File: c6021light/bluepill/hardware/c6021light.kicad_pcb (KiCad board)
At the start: 2 copper layers, 100 x 50 mm, 82 parts, among them J1 Barrel_Jack_Switch, J10 Conn_01x02, J11 Conn_01x02, J12 XpressNet, J2 Conn_02x04_Odd_Even, J3 Conn_02x16_Row_Letter_First, J30 Loconet, J31 Conn_01x02, J32 Conn_01x02, J4 Conn_01x02, J5 Grove I2C, J50 USB_B_Micro, J51 Conn_01x06, J52 Debug UART, J6 Conn_01x02, J7 Conn_01x02, J8 RJ45, Q30 BC337, Q31 BC547, Q32 BC547, SW1 SW_Push, U1 L7805, U10 SN75176, U2 L7808, U3 MCP2562, U30 LM393, U4 ISO1050DUB, U50 CH340C

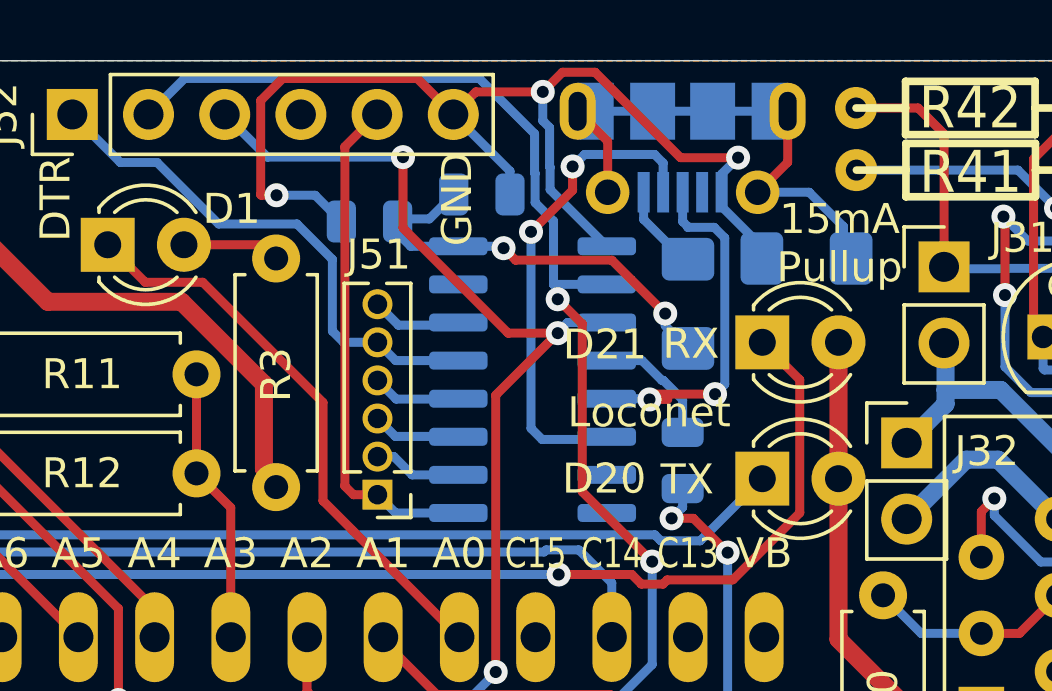
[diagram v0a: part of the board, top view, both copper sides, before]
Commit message: remove some unneccessary resistors
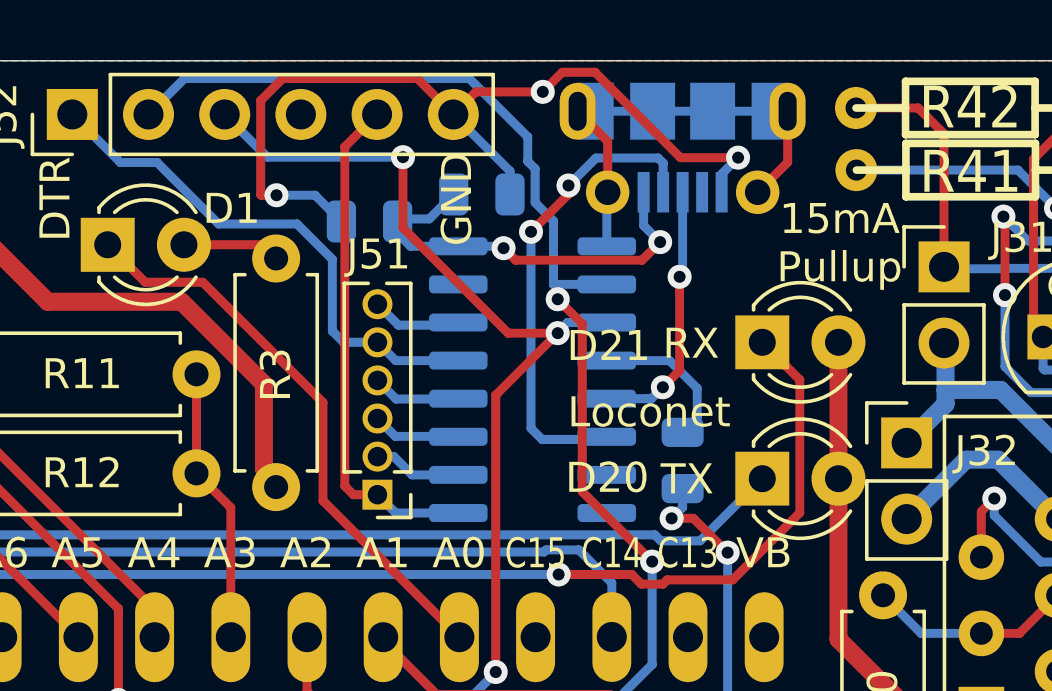
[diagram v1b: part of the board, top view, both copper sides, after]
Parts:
- removed R50, R51: 0, Resistor_SMD:R_1206_3216Metric_Pad1.42x1.75mm_HandSolder
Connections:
- J50 pad 1: Net-(J50-Pad1) -> Net-(C50-Pad1)
- J50 pad 6: Net-(J50-Pad6) -> GND
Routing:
- net Net-(J50-Pad6): track 17.1 -> 0.00 mm
- net GND: track 242.1 -> 247.7 mm
- net Net-(J50-Pad3): track 12.3 -> 8.84 mm
- net Net-(J50-Pad1): track 2.74 -> 0.00 mm
- net Net-(C52-Pad1): track 4.16 -> 5.07 mm
